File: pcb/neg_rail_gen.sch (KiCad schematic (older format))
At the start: 48 parts

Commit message: clean up
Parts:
- removed C?: 47u, symbol Device:CP
- removed C? (x4): 100u, symbol Device:CP
- removed C? (x2): 2u, symbol Device:C
- removed C?: 82p, symbol Device:C
- removed C? (x3): 10u, symbol Device:C
- removed C?: 0.1u, symbol Device:C
- removed C?: 1000u, symbol Device:CP
- removed D?: 1N5817, Diode_THT:D_DO-41_SOD81_P10.16mm_Horizontal, symbol Diode:1N5817
- removed D?: 1N5819, Diode_THT:D_DO-41_SOD81_P10.16mm_Horizontal, symbol Diode:1N5819
- removed L?: 10u, symbol Device:L
- removed L?: 22u, symbol Device:L
- removed L? (x2): L_Core_Ferrite, symbol Device:L_Core_Ferrite
- removed L?: 88u, symbol Device:L
- removed L?: 1u, symbol Device:L
- removed R?: 130k, symbol Device:R
- removed R?: 300k, symbol Device:R
- removed R?: 10k, symbol Device:R
- removed R? (x3): XXX, symbol Device:R
- removed U?: TPS6735ID, SOIC127P599X175-8N, symbol TPS6735ID:TPS6735ID
- removed U?: MC33063AD, Package_SO:SOIC-8_3.9x4.9mm_P1.27mm, symbol Regulator_Switching:MC33063AD
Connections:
- wire segments 114 -> 49
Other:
- moved on the sheet: C?, D?, L?, R?, U?

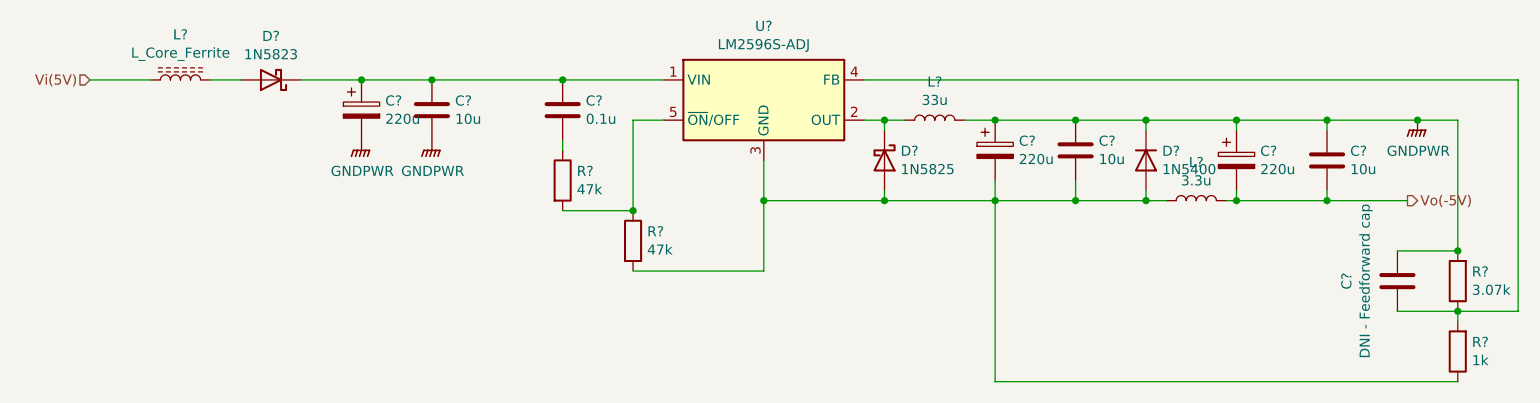
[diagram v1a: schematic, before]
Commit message: Define pin map, clean up schematic
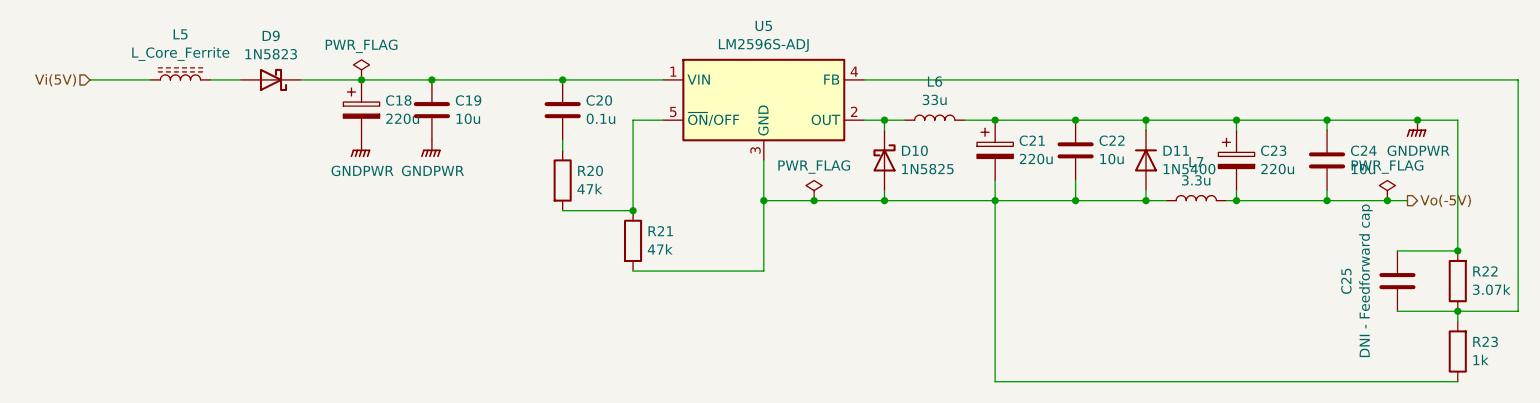
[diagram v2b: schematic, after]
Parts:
- gave numbers to parts that had none: 19
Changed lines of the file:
@@
 $Descr A4 11693 8268
 encoding utf-8
-Sheet 3 3
+Sheet 3 6
 Title ""
 Date ""
@@
 $EndDescr
 $Comp
-L Diode:1N5822 D?
+L Diode:1N5822 D9
 U 1 1 5FD6BB54
 P 3350 3400
-F 0 "D?" H 3350 3183 50  0000 C CNN
+F 0 "D9" H 3350 3183 50  0000 C CNN
 F 1 "1N5823" H 3350 3274 50  0000 C CNN
 F 2 "Diode_THT:D_DO-201AD_P15.24mm_Horizontal" H 3350 3225 50  0001 C CNN
@@
 	5300 3400 4800 3400
 $Comp
-L Device:L L?
+L Device:L L6
 U 1 1 5FD6EA52
 P 6650 3600
-F 0 "L?" V 6840 3600 50  0000 C CNN
+F 0 "L6" V 6840 3600 50  0000 C CNN
 F 1 "33u" V 6749 3600 50  0000 C CNN
 F 2 "" H 6650 3600 50  0001 C CNN
@@
 	6300 3600 6400 3600
 $Comp
-L Device:CP C?
+L Device:CP C21
 U 1 1 5FD71007
 P 6950 3750
-F 0 "C?" H 7068 3796 50  0000 L CNN
+F 0 "C21" H 7068 3796 50  0000 L CNN
 F 1 "220u" H 7068 3705 50  0000 L CNN
 F 2 "" H 6988 3600 50  0001 C CNN
@@
 $EndComp
 $Comp
-L Device:C C?
+L Device:C C22
 U 1 1 5FD73530
 P 7350 3750
-F 0 "C?" H 7235 3704 50  0000 R CNN
+F 0 "C22" H 7235 3704 50  0000 R CNN
 F 1 "10u" H 7235 3795 50  0000 R CNN
 F 2 "" H 7388 3600 50  0001 C CNN
@@
 $EndComp
 $Comp
-L Device:L L?
+L Device:L L7
 U 1 1 5FD79ECF
 P 7950 4000
-F 0 "L?" V 8140 4000 50  0000 C CNN
+F 0 "L7" V 8140 4000 50  0000 C CNN
 F 1 "3.3u" V 8049 4000 50  0000 C CNN
 F 2 "" H 7950 4000 50  0001 C CNN
@@
 Connection ~ 8150 3600
 $Comp
-L Device:C C?
+L Device:C C24
 U 1 1 5FD79EE0
 P 8600 3800
-F 0 "C?" H 8485 3754 50  0000 R CNN
+F 0 "C24" H 8485 3754 50  0000 R CNN
 F 1 "10u" H 8485 3845 50  0000 R CNN
 F 2 "" H 8638 3650 50  0001 C CNN
@@
 	8600 3600 8150 3600
 $Comp
-L Diode:1N5822 D?
+L Diode:1N5822 D10
 U 1 1 5FD8306A
 P 6400 3800
-F 0 "D?" V 6354 3880 50  0000 L CNN
+F 0 "D10" V 6354 3880 50  0000 L CNN
 F 1 "1N5825" V 6445 3880 50  0000 L CNN
 F 2 "Diode_THT:D_DO-201AD_P15.24mm_Horizontal" H 6400 3625 50  0001 C CNN
@@
 	6400 3600 6500 3600
 $Comp
-L Device:CP C?
+L Device:CP C18
 U 1 1 5FD8CD2C
 P 3800 3550
-F 0 "C?" H 3918 3596 50  0000 L CNN
+F 0 "C18" H 3918 3596 50  0000 L CNN
 F 1 "220u" H 3918 3505 50  0000 L CNN
 F 2 "" H 3838 3400 50  0001 C CNN
@@
 $EndComp
 $Comp
-L power:GNDPWR #PWR?
+L power:GNDPWR #PWR0139
 U 1 1 5FD8CD32
 P 4150 3700
-F 0 "#PWR?" H 4150 3500 50  0001 C CNN
+F 0 "#PWR0139" H 4150 3500 50  0001 C CNN
 F 1 "GNDPWR" H 4154 3546 50  0000 C CNN
 F 2 "" H 4150 3650 50  0001 C CNN
@@
 $EndComp
 $Comp
-L power:GNDPWR #PWR?
+L power:GNDPWR #PWR0140
 U 1 1 5FD8CD38
 P 3800 3700
-F 0 "#PWR?" H 3800 3500 50  0001 C CNN
+F 0 "#PWR0140" H 3800 3500 50  0001 C CNN
 F 1 "GNDPWR" H 3804 3546 50  0000 C CNN
 F 2 "" H 3800 3650 50  0001 C CNN
@@
 $EndComp
 $Comp
-L Device:C C?
+L Device:C C19
 U 1 1 5FD8CD3E
 P 4150 3550
-F 0 "C?" H 4265 3596 50  0000 L CNN
+F 0 "C19" H 4265 3596 50  0000 L CNN
 F 1 "10u" H 4265 3505 50  0000 L CNN
 F 2 "" H 4188 3400 50  0001 C CNN
@@
 P 2900 3400
 AR Path="/5FD8CD48" Ref="L?"  Part="1"
-AR Path="/5FC35984/5FD8CD48" Ref="L?"  Part="1"
-F 0 "L?" V 3125 3400 50  0000 C CNN
+AR Path="/5FC35984/5FD8CD48" Ref="L5"  Part="1"
+F 0 "L5" V 3125 3400 50  0000 C CNN
 F 1 "L_Core_Ferrite" V 3034 3400 50  0000 C CNN
 F 2 "" H 2900 3400 50  0001 C CNN
@@
 	0    -1   -1   0
 $EndComp
-Wire Wire Line
-	2750 3400 2450 3400
 Connection ~ 3800 3400
 Wire Wire Line
@@
 	5300 3600 5150 3600
 Wire Wire Line
-	5800 4000 6400 4000
+	5800 4000 6050 4000
 Wire Wire Line
 	6400 3950 6400 4000
@@
 	8600 4000 8600 3950
 Wire Wire Line
-	8600 4000 9000 4000
+	8600 4000 8900 4000
 Connection ~ 8600 4000
 $Comp
-L Device:CP C?
+L Device:CP C23
 U 1 1 5FDC37D7
 P 8150 3800
-F 0 "C?" H 8268 3846 50  0000 L CNN
+F 0 "C23" H 8268 3846 50  0000 L CNN
 F 1 "220u" H 8268 3755 50  0000 L CNN
 F 2 "" H 8188 3650 50  0001 C CNN
@@
 	8100 4000 8150 4000
 $Comp
-L power:GNDPWR #PWR?
+L power:GNDPWR #PWR0141
 U 1 1 5FDC93D0
 P 9050 3600
-F 0 "#PWR?" H 9050 3400 50  0001 C CNN
+F 0 "#PWR0141" H 9050 3400 50  0001 C CNN
 F 1 "GNDPWR" H 9054 3446 50  0000 C CNN
 F 2 "" H 9050 3550 50  0001 C CNN
@@
 	7350 4000 7700 4000
 $Comp
-L Diode:1N5400 D?
+L Diode:1N5400 D11
 U 1 1 5FDD5015
 P 7700 3800
-F 0 "D?" V 7654 3880 50  0000 L CNN
+F 0 "D11" V 7654 3880 50  0000 L CNN
 F 1 "1N5400" V 7745 3880 50  0000 L CNN
 F 2 "Diode_THT:D_DO-201AD_P15.24mm_Horizontal" H 7700 3625 50  0001 C CNN
@@
 	7700 4000 7800 4000
 $Comp
-L Device:R R?
+L Device:R R21
 U 1 1 5FDDC2C2
 P 5150 4200
-F 0 "R?" H 5220 4246 50  0000 L CNN
+F 0 "R21" H 5220 4246 50  0000 L CNN
 F 1 "47k" H 5220 4155 50  0000 L CNN
 F 2 "" V 5080 4200 50  0001 C CNN
@@
 $EndComp
 $Comp
-L Device:R R?
+L Device:R R20
 U 1 1 5FDDC644
 P 4800 3900
-F 0 "R?" H 4870 3946 50  0000 L CNN
+F 0 "R20" H 4870 3946 50  0000 L CNN
 F 1 "47k" H 4870 3855 50  0000 L CNN
 F 2 "" V 4730 3900 50  0001 C CNN
@@
 $EndComp
 $Comp
-L Regulator_Switching:LM2596S-ADJ U?
+L Regulator_Switching:LM2596S-ADJ U5
 U 1 1 5FD69A66
 P 5800 3500
-F 0 "U?" H 5800 3867 50  0000 C CNN
+F 0 "U5" H 5800 3867 50  0000 C CNN
 F 1 "LM2596S-ADJ" H 5800 3776 50  0000 C CNN
 F 2 "Package_TO_SOT_SMD:TO-263-5_TabPin3" H 5850 3250 50  0001 L CIN
@@
 Connection ~ 5800 4000
 $Comp
-L Device:C C?
+L Device:C C20
 U 1 1 5FDEA8C9
 P 4800 3550
-F 0 "C?" H 4915 3596 50  0000 L CNN
+F 0 "C20" H 4915 3596 50  0000 L CNN
 F 1 "0.1u" H 4915 3505 50  0000 L CNN
 F 2 "" H 4838 3400 50  0001 C CNN
@@
 	6950 3600 7350 3600
 $Comp
-L Device:C C?
+L Device:C C25
 U 1 1 5FE0D49B
 P 8950 4400
-F 0 "C?" V 9202 4400 50  0000 C CNN
+F 0 "C25" V 9202 4400 50  0000 C CNN
 F 1 "DNI - Feedforward cap" V 9111 4400 50  0000 C CNN
 F 2 "" H 8988 4250 50  0001 C CNN
@@
 $EndComp
 $Comp
-L Device:R R?
+L Device:R R22
 U 1 1 5FE19832
 P 9250 4400
-F 0 "R?" H 9180 4354 50  0000 R CNN
+F 0 "R22" H 9180 4354 50  0000 R CNN
 F 1 "3.07k" H 9180 4445 50  0000 R CNN
 F 2 "" V 9180 4400 50  0001 C CNN
@@
 	6950 4900 9250 4900
 $Comp
-L Device:R R?
+L Device:R R23
 U 1 1 5FE1B1CA
 P 9250 4750
-F 0 "R?" H 9180 4704 50  0000 R CNN
+F 0 "R23" H 9180 4704 50  0000 R CNN
 F 1 "1k" H 9180 4795 50  0000 R CNN
 F 2 "" V 9180 4750 50  0001 C CNN
@@
 Wire Wire Line
 	8950 4550 9250 4550
+$Comp
+L power:PWR_FLAG #FLG0102
+U 1 1 5FE36453
+P 8900 4000
+F 0 "#FLG0102" H 8900 4075 50  0001 C CNN
+F 1 "PWR_FLAG" H 8900 4173 50  0000 C CNN
+F 2 "" H 8900 4000 50  0001 C CNN
+F 3 "~" H 8900 4000 50  0001 C CNN
+	1    8900 4000
+	1    0    0    -1
+$EndComp
+Connection ~ 8900 4000
+Wire Wire Line
+	8900 4000 9000 4000
+Wire Wire Line
+	2450 3400 2750 3400
+$Comp
+L power:PWR_FLAG #FLG0104
+U 1 1 5FE3E0B5
+P 3800 3400
+F 0 "#FLG0104" H 3800 3475 50  0001 C CNN
+F 1 "PWR_FLAG" H 3800 3573 50  0000 C CNN
+F 2 "" H 3800 3400 50  0001 C CNN
+F 3 "~" H 3800 3400 50  0001 C CNN
+	1    3800 3400
+	1    0    0    -1
+$EndComp
+$Comp
+L power:PWR_FLAG #FLG0105
+U 1 1 5FE3F4DD
+P 6050 4000
+F 0 "#FLG0105" H 6050 4075 50  0001 C CNN
+F 1 "PWR_FLAG" H 6050 4173 50  0000 C CNN
+F 2 "" H 6050 4000 50  0001 C CNN
+F 3 "~" H 6050 4000 50  0001 C CNN
+	1    6050 4000
+	1    0    0    -1
+$EndComp
+Connection ~ 6050 4000
+Wire Wire Line
+	6050 4000 6400 4000
 $EndSCHEMATC

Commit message: clean up ERC, more DFT stuff, started sigma delta adc
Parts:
- added TP54, TP55, TP56, TP57, TP58: TestPoint, symbol Connector:TestPoint
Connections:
- net GNDPWR: now also TP58.1
- net Vo(-5V): now also TP57.1
- net at C18.1, C19.1, C20.1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: now also TP54.1
- net at D10.1 (K), L6.1, U5.2 (OUT): now also TP56.1
- net at C25.1, R22.1, R23.2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: now also TP55.1
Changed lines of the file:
@@
 $Descr A4 11693 8268
 encoding utf-8
-Sheet 3 6
+Sheet 3 7
 Title ""
 Date ""
@@
 $EndComp
 Wire Wire Line
-	5300 3400 4800 3400
+	5300 3400 5150 3400
 $Comp
 L Device:L L6
@@
 Connection ~ 9250 4550
 Wire Wire Line
-	6300 3400 9550 3400
+	6300 3400 6400 3400
 Wire Wire Line
 	8950 4250 9250 4250
@@
 Connection ~ 8900 4000
 Wire Wire Line
-	8900 4000 9000 4000
+	8900 4000 8950 4000
 Wire Wire Line
 	2450 3400 2750 3400
@@
 Wire Wire Line
 	6050 4000 6400 4000
+$Comp
+L Connector:TestPoint TP54
+U 1 1 609BE548
+P 5150 3400
+F 0 "TP54" H 5208 3518 50  0000 L CNN
+F 1 "TestPoint" H 5208 3427 50  0000 L CNN
+F 2 "" H 5350 3400 50  0001 C CNN
+F 3 "~" H 5350 3400 50  0001 C CNN
+	1    5150 3400
+	1    0    0    -1
+$EndComp
+Connection ~ 5150 3400
+Wire Wire Line
+	5150 3400 4800 3400
+$Comp
+L Connector:TestPoint TP55
+U 1 1 609BF7FB
+P 6400 3400
+F 0 "TP55" H 6458 3518 50  0000 L CNN
+F 1 "TestPoint" H 6458 3427 50  0000 L CNN
+F 2 "" H 6600 3400 50  0001 C CNN
+F 3 "~" H 6600 3400 50  0001 C CNN
+	1    6400 3400
+	1    0    0    -1
+$EndComp
+Connection ~ 6400 3400
+Wire Wire Line
+	6400 3400 9550 3400
+$Comp
+L Connector:TestPoint TP56
+U 1 1 609C01D4
+P 6400 3600
+F 0 "TP56" H 6458 3718 50  0000 L CNN
+F 1 "TestPoint" H 6458 3627 50  0000 L CNN
+F 2 "" H 6600 3600 50  0001 C CNN
+F 3 "~" H 6600 3600 50  0001 C CNN
+	1    6400 3600
+	1    0    0    -1
+$EndComp
+$Comp
+L Connector:TestPoint TP57
+U 1 1 609C0F52
+P 8950 4000
+F 0 "TP57" H 9008 4118 50  0000 L CNN
+F 1 "TestPoint" H 9008 4027 50  0000 L CNN
+F 2 "" H 9150 4000 50  0001 C CNN
+F 3 "~" H 9150 4000 50  0001 C CNN
+	1    8950 4000
+	1    0    0    -1
+$EndComp
+Connection ~ 8950 4000
+Wire Wire Line
+	8950 4000 9000 4000
+$Comp
+L Connector:TestPoint TP58
+U 1 1 609C48B5
+P 9050 3600
+F 0 "TP58" H 9108 3718 50  0000 L CNN
+F 1 "TestPoint" H 9108 3627 50  0000 L CNN
+F 2 "" H 9250 3600 50  0001 C CNN
+F 3 "~" H 9250 3600 50  0001 C CNN
+	1    9050 3600
+	1    0    0    -1
+$EndComp
 $EndSCHEMATC

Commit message: started assigning footprints
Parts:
- C18, C21, C23: footprint (none) -> Capacitor_Tantalum_SMD:CP_EIA-7343-20_Kemet-V_Pad2.25x2.55mm_HandSolder
- C19, C20, C22, C24, C25: footprint (none) -> Capacitor_SMD:C_0805_2012Metric_Pad1.15x1.40mm_HandSolder
- R20, R21, R22, R23: footprint (none) -> Resistor_SMD:R_0805_2012Metric_Pad1.20x1.40mm_HandSolder
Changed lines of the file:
@@
 F 0 "C21" H 7068 3796 50  0000 L CNN
 F 1 "220u" H 7068 3705 50  0000 L CNN
-F 2 "" H 6988 3600 50  0001 C CNN
+F 2 "Capacitor_Tantalum_SMD:CP_EIA-7343-20_Kemet-V_Pad2.25x2.55mm_HandSolder" H 6988 3600 50  0001 C CNN
 F 3 "~" H 6950 3750 50  0001 C CNN
 	1    6950 3750
@@
 F 0 "C22" H 7235 3704 50  0000 R CNN
 F 1 "10u" H 7235 3795 50  0000 R CNN
-F 2 "" H 7388 3600 50  0001 C CNN
+F 2 "Capacitor_SMD:C_0805_2012Metric_Pad1.15x1.40mm_HandSolder" H 7388 3600 50  0001 C CNN
 F 3 "~" H 7350 3750 50  0001 C CNN
 	1    7350 3750
@@
 F 0 "C24" H 8485 3754 50  0000 R CNN
 F 1 "10u" H 8485 3845 50  0000 R CNN
-F 2 "" H 8638 3650 50  0001 C CNN
+F 2 "Capacitor_SMD:C_0805_2012Metric_Pad1.15x1.40mm_HandSolder" H 8638 3650 50  0001 C CNN
 F 3 "~" H 8600 3800 50  0001 C CNN
 	1    8600 3800
@@
 F 0 "C18" H 3918 3596 50  0000 L CNN
 F 1 "220u" H 3918 3505 50  0000 L CNN
-F 2 "" H 3838 3400 50  0001 C CNN
+F 2 "Capacitor_Tantalum_SMD:CP_EIA-7343-20_Kemet-V_Pad2.25x2.55mm_HandSolder" H 3838 3400 50  0001 C CNN
 F 3 "~" H 3800 3550 50  0001 C CNN
 	1    3800 3550
@@
 F 0 "C19" H 4265 3596 50  0000 L CNN
 F 1 "10u" H 4265 3505 50  0000 L CNN
-F 2 "" H 4188 3400 50  0001 C CNN
+F 2 "Capacitor_SMD:C_0805_2012Metric_Pad1.15x1.40mm_HandSolder" H 4188 3400 50  0001 C CNN
 F 3 "~" H 4150 3550 50  0001 C CNN
 	1    4150 3550
@@
 F 0 "C23" H 8268 3846 50  0000 L CNN
 F 1 "220u" H 8268 3755 50  0000 L CNN
-F 2 "" H 8188 3650 50  0001 C CNN
+F 2 "Capacitor_Tantalum_SMD:CP_EIA-7343-20_Kemet-V_Pad2.25x2.55mm_HandSolder" H 8188 3650 50  0001 C CNN
 F 3 "~" H 8150 3800 50  0001 C CNN
 	1    8150 3800
@@
 F 0 "R21" H 5220 4246 50  0000 L CNN
 F 1 "47k" H 5220 4155 50  0000 L CNN
-F 2 "" V 5080 4200 50  0001 C CNN
+F 2 "Resistor_SMD:R_0805_2012Metric_Pad1.20x1.40mm_HandSolder" V 5080 4200 50  0001 C CNN
 F 3 "~" H 5150 4200 50  0001 C CNN
 	1    5150 4200
@@
 F 0 "R20" H 4870 3946 50  0000 L CNN
 F 1 "47k" H 4870 3855 50  0000 L CNN
-F 2 "" V 4730 3900 50  0001 C CNN
+F 2 "Resistor_SMD:R_0805_2012Metric_Pad1.20x1.40mm_HandSolder" V 4730 3900 50  0001 C CNN
 F 3 "~" H 4800 3900 50  0001 C CNN
 	1    4800 3900
@@
 F 0 "C20" H 4915 3596 50  0000 L CNN
 F 1 "0.1u" H 4915 3505 50  0000 L CNN
-F 2 "" H 4838 3400 50  0001 C CNN
+F 2 "Capacitor_SMD:C_0805_2012Metric_Pad1.15x1.40mm_HandSolder" H 4838 3400 50  0001 C CNN
 F 3 "~" H 4800 3550 50  0001 C CNN
 	1    4800 3550
@@
 F 0 "C25" V 9202 4400 50  0000 C CNN
 F 1 "DNI - Feedforward cap" V 9111 4400 50  0000 C CNN
-F 2 "" H 8988 4250 50  0001 C CNN
+F 2 "Capacitor_SMD:C_0805_2012Metric_Pad1.15x1.40mm_HandSolder" H 8988 4250 50  0001 C CNN
 F 3 "~" H 8950 4400 50  0001 C CNN
 	1    8950 4400
@@
 F 0 "R22" H 9180 4354 50  0000 R CNN
 F 1 "3.07k" H 9180 4445 50  0000 R CNN
-F 2 "" V 9180 4400 50  0001 C CNN
+F 2 "Resistor_SMD:R_0805_2012Metric_Pad1.20x1.40mm_HandSolder" V 9180 4400 50  0001 C CNN
 F 3 "~" H 9250 4400 50  0001 C CNN
 	1    9250 4400
@@
 F 0 "R23" H 9180 4704 50  0000 R CNN
 F 1 "1k" H 9180 4795 50  0000 R CNN
-F 2 "" V 9180 4750 50  0001 C CNN
+F 2 "Resistor_SMD:R_0805_2012Metric_Pad1.20x1.40mm_HandSolder" V 9180 4750 50  0001 C CNN
 F 3 "~" H 9250 4750 50  0001 C CNN
 	1    9250 4750
